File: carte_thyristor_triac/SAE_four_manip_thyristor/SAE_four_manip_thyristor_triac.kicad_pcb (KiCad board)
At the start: 2 copper layers, 22 parts, among them J2 Conn_01x02_Pin, J3 Conn_01x02_Pin, J5 Jack-DC, SW1 SW_Push, U1 4N35, U4 L78L05_TO92, U5 4N35, U6 4N35

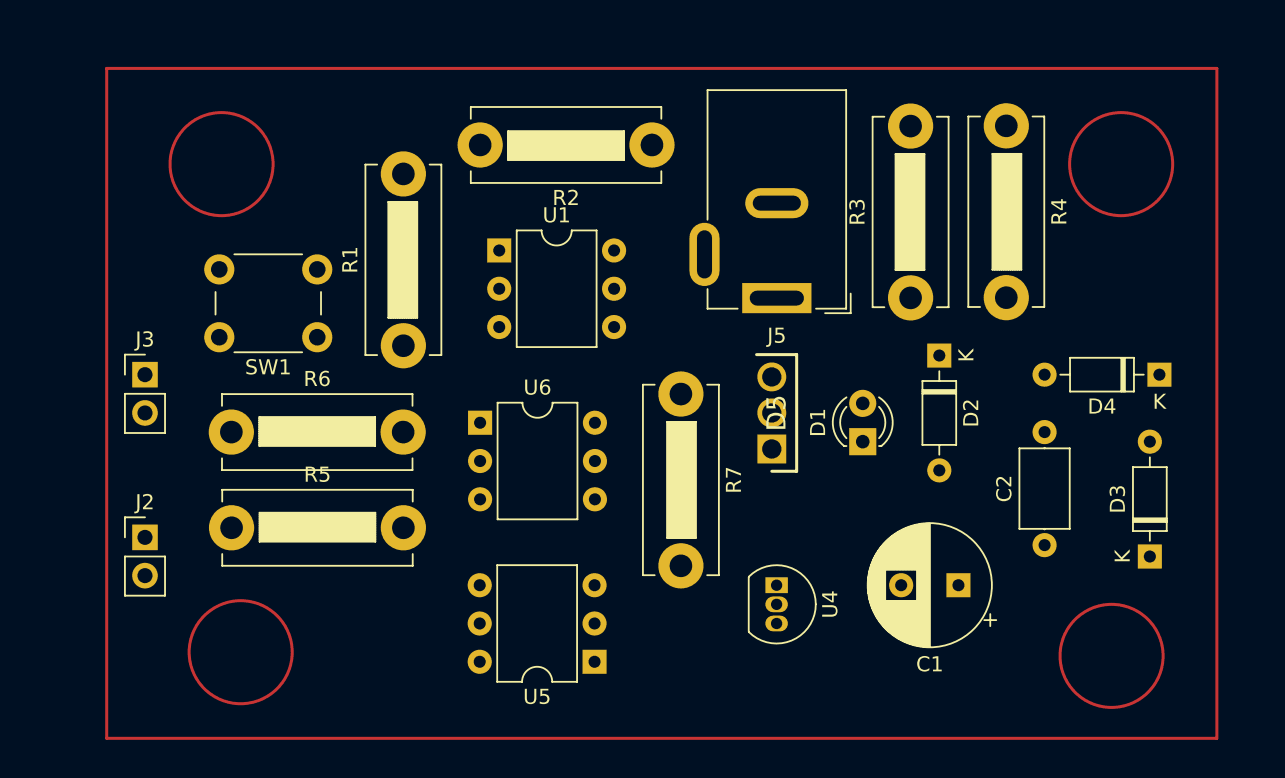
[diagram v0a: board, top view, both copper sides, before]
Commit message: update thyristor triac et docs
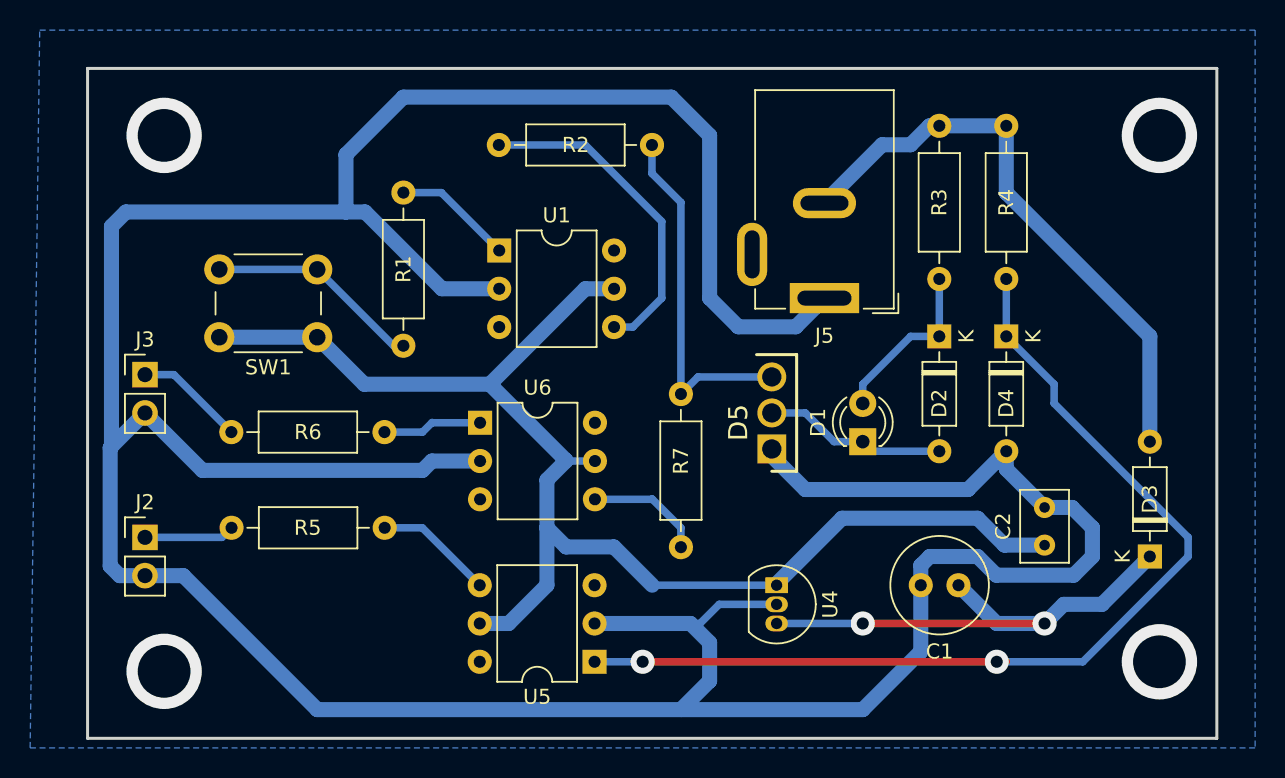
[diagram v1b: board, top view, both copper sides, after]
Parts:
- C1: footprint Capacitor_THT:CP_Radial_D8.0mm_P3.80mm -> Capacitor_THT:C_Radial_D6.3mm_H5.0mm_P2.50mm
- C2: footprint Capacitor_THT:C_Axial_L5.1mm_D3.1mm_P7.50mm_Horizontal -> Capacitor_THT:C_Rect_L4.6mm_W3.0mm_P2.50mm_MKS02_FKP02
- D5: footprint componentsearchengine_com:C106DG -> SamacSys_Parts:C106DG
- J5: footprint Connector_BarrelJack:BarrelJack_GCT_DCJ200-10-A_Horizontal -> SamacSys_Parts:BarrelJack_GCT_DCJ200-10-A_Horizontal_3D
- R1, R2, R3, R4, R5, R6, R7: footprint Resistor_THT:R_Bare_Metal_Element_L12.4mm_W4.8mm_P11.40mm -> Resistor_THT:R_Axial_DIN0207_L6.3mm_D2.5mm_P10.16mm_Horizontal
- moved D4 10.5 mm to (101.0, 71.8), turned to -90 degrees
- moved J5 3.16 mm to (88.9, 69.2)
- moved R3 2.28 mm to (96.5, 67.9)
- moved D2 1.27 mm to (96.5, 71.8)
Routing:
- net GND: track 0.00 -> 260.7 mm
- net +5V: track 0.00 -> 90.6 mm
- net Net-(D4-K): track 0.00 -> 66.3 mm, vias 0 -> 2
- net VIN: track 0.00 -> 39.1 mm
- net Net-(D3-K): track 0.00 -> 33.4 mm, vias 0 -> 2
- net Net-(D5-Pad3): track 0.00 -> 23.8 mm
- net Net-(R2-Pad2): track 0.00 -> 22.0 mm
- net Net-(R1-Pad1): track 0.00 -> 14.3 mm
- net Net-(D1-K): track 0.00 -> 12.2 mm
- net Net-(D1-A): track 0.00 -> 11.5 mm
- net Net-(R1-Pad2): track 0.00 -> 7.95 mm
- net Net-(R5-Pad2): track 0.00 -> 7.88 mm
- net Net-(R7-Pad2): track 0.00 -> 7.79 mm
- net Net-(J3-Pin_1): track 0.00 -> 7.31 mm
- net Net-(R6-Pad2): track 0.00 -> 6.61 mm
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- added copper zone on B.Cu, net GND
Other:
- board outline added: 74.9 x 44.4 mm
